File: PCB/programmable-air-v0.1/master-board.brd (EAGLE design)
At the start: 101.7 x 50.9 mm, 14 parts, among them J1 POWER_JACKTOE, Q1 600mA/40V, Q2 600mA/40V

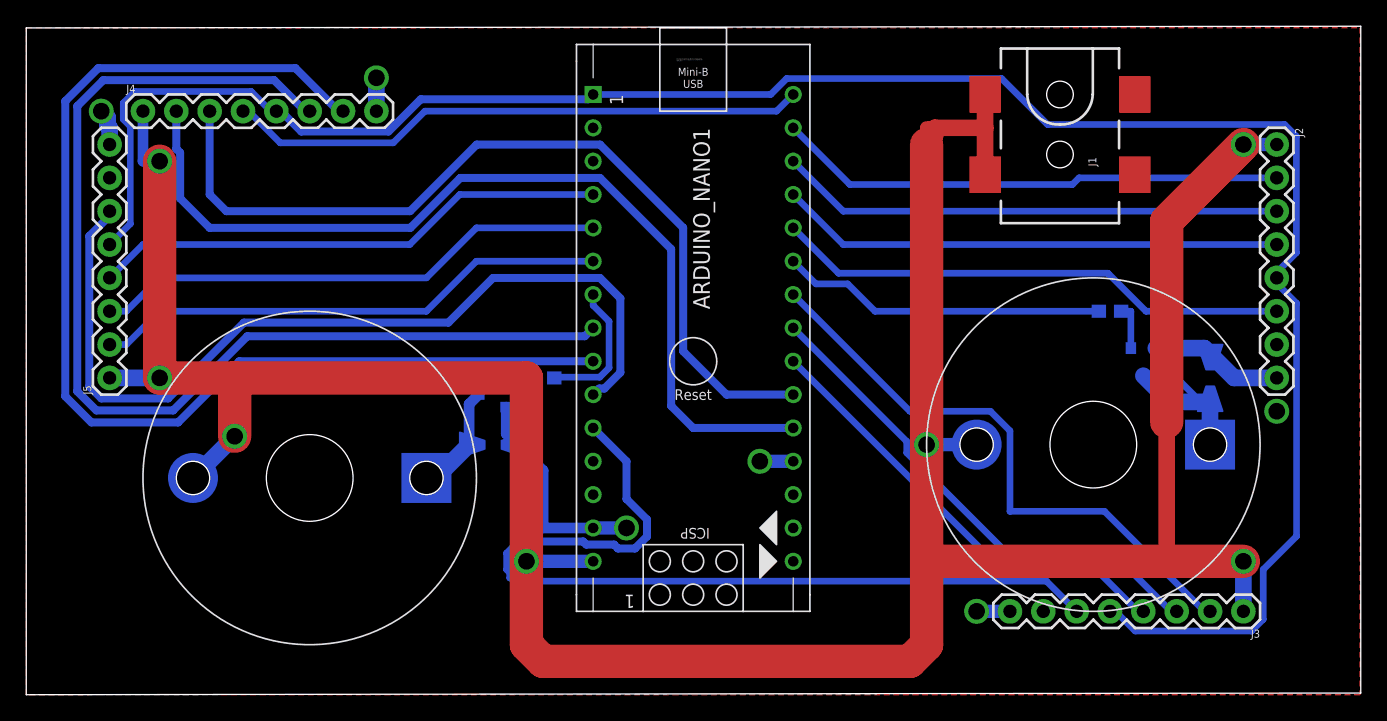
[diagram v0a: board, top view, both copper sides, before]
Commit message: Started work on slave PCB. Made changes to master pcb after testing
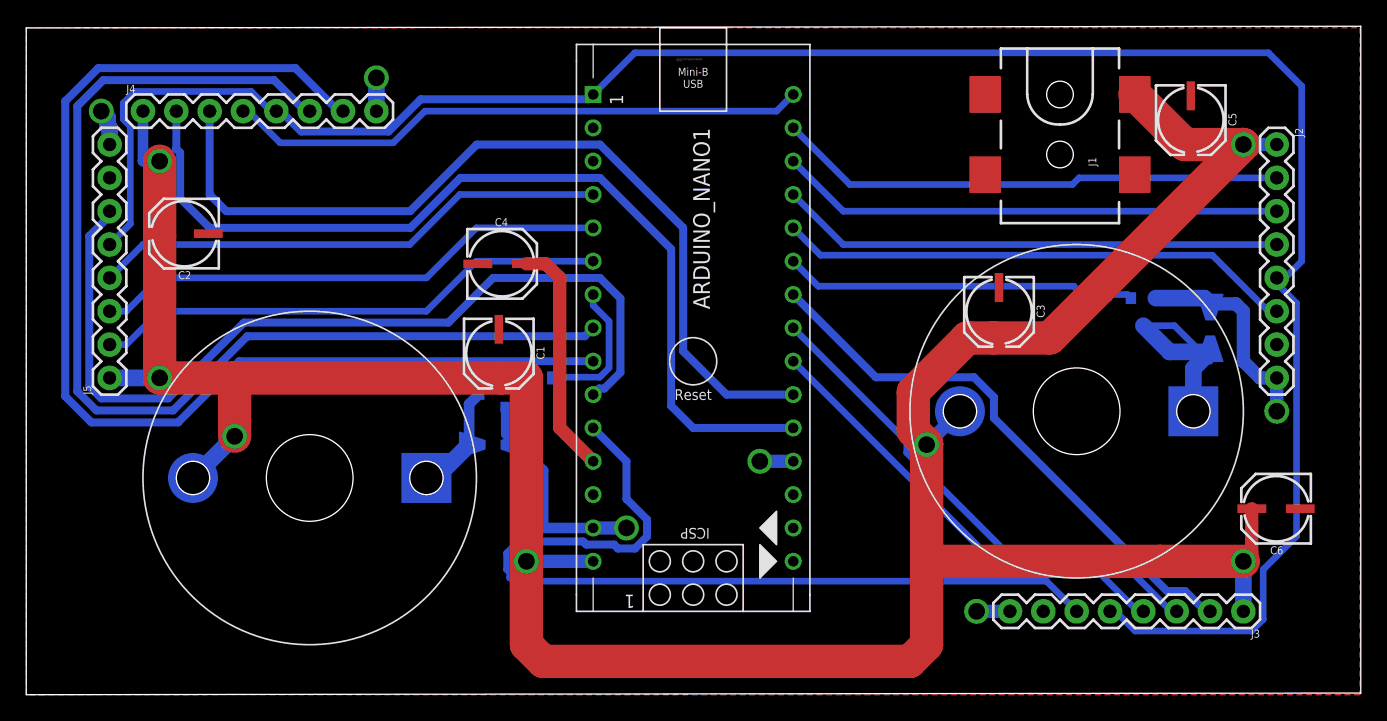
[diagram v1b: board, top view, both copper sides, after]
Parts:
- added C1, C2, C3, C4, C5, C6: 22uF, SparkFun-Capacitors:PANASONIC_C
- moved Q1 3.81 mm to (85.1, 29.2)
- moved U$4 3.81 mm to (90.2, 27.9)
- moved U$2 2.84 mm to (80.0, 21.6)
- moved R2 1.80 mm to (81.3, 30.5)
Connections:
- removed net 5V: ARDUINO_NANO1.12
- new net N$20: ARDUINO_NANO1.12, C4.+
- net GND: now also C1.-, C2.-, C3.-, C4.-, C5.-, C6.-, J1.GND, J1.P$4; no longer J1.VIN0
- net VIN: now also C1.+, C2.+, C3.+, C5.+, C6.+, J1.VIN0; no longer J1.GND, J1.P$4
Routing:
- net N$20: track 0.00 -> 18.0 mm
- net VIN: track 238.4 -> 221.9 mm
- net GND: track 37.3 -> 43.6 mm
- net N$13: track 157.9 -> 162.7 mm
- net N$9: track 45.3 -> 42.7 mm
- net N$1: track 24.9 -> 23.1 mm
- net N$6: track 15.4 -> 17.2 mm
- net N$7: track 3.55 -> 2.12 mm

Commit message: PCB v0.11 master ready for production
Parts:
- removed Q1, Q2: 600mA/40V, SparkFun-DiscreteSemi:SOT23-3
- added U$5, U$6: TIP120-TO220, programmable-air-components:TO220
- moved C3 23.0 mm to (63.5, 8.89)
- moved R2 19.1 mm to (62.2, 31.1)
- moved U$4 15.3 mm to (80.0, 16.5), turned to 0 degrees
- moved U$3 9.09 mm to (26.7, 21.0)
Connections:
- net GND: now also U$5.P$3, U$6.P$3; no longer Q1.2, Q2.2, U$3.P$2, U$4.P$2
- net N$2: now also U$6.P$1; no longer Q2.1
- net N$5: now also U$3.P$2, U$6.P$2; no longer Q2.3, U$3.P$1
- net N$6: now also U$4.P$2, U$5.P$2; no longer Q1.3, U$4.P$1
- net N$7: now also U$5.P$1; no longer Q1.1
- net VIN: now also U$3.P$1, U$4.P$1
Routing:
- net N$15: track 68.1 -> 42.6 mm
- net N$6: track 17.2 -> 39.5 mm
- net N$2: track 2.09 -> 22.0 mm
- net N$1: track 23.1 -> 3.75 mm
- net N$5: track 8.42 -> 21.2 mm
- net GND: track 43.6 -> 50.9 mm, vias 6 -> 7
- net VIN: track 221.9 -> 229.0 mm
- net N$9: track 42.7 -> 49.0 mm
- net N$4: track 38.7 -> 44.7 mm
- net N$3: track 34.6 -> 40.5 mm
- net N$22: track 39.5 -> 43.6 mm
- net N$23: track 38.4 -> 40.5 mm
- net N$24: track 38.4 -> 39.5 mm
- net N$7: track 2.12 -> 2.63 mm

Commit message: Forgot to add 5V input to slave boards
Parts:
- moved C6 0.90 mm to (95.9, 14.6), turned to 270 degrees
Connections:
- removed net N$12: ARDUINO_NANO1.9, J4.7
- net N$20: now also J2.7, J3.7, J4.7, J5.7
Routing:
- net N$20: track 18.0 -> 164.9 mm, vias 0 -> 2
- net N$12: track 89.0 -> 0.00 mm
- net GND: track 50.9 -> 23.8 mm, vias 7 -> 8
- net N$11: track 83.7 -> 85.0 mm
- net VIN: track 229.0 -> 228.7 mm, vias 7 -> 8
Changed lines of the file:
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@@
 <setting verticaltext="up"/>
 </settings>
-<grid distance="25" unitdist="mil" unit="mil" style="lines" multiple="1" display="yes" altdistance="5" altunitdist="mil" altunit="mil"/>
+<grid distance="50" unitdist="mil" unit="mil" style="lines" multiple="1" display="yes" altdistance="5" altunitdist="mil" altunit="mil"/>
 <layers>
 <layer number="1" name="Top" color="4" fill="1" visible="yes" active="yes"/>
@@
 <attribute name="PROD_ID" value="CAP-08618" x="88.9" y="43.815" size="1.778" layer="27" rot="R270" display="off"/>
 </element>
-<element name="C6" library="SparkFun-Capacitors" package="PANASONIC_C" value="22uF" x="95.25" y="13.97" rot="R180">
-<attribute name="PROD_ID" value="CAP-08618" x="95.25" y="13.97" size="1.778" layer="27" rot="R180" display="off"/>
+<element name="C6" library="SparkFun-Capacitors" package="PANASONIC_C" value="22uF" x="95.885" y="14.605" rot="R270">
+<attribute name="PROD_ID" value="CAP-08618" x="95.885" y="14.605" size="1.778" layer="27" rot="R270" display="off"/>
 </element>
 <element name="U$5" library="programmable-air-components" package="TO220" value="TIP120-TO220" x="65.405" y="33.655"/>
@@
 <contactref element="U$6" pad="P$3"/>
 <contactref element="U$5" pad="P$3"/>
-<wire x1="93.345" y1="24.13" x2="94.9325" y2="24.13" width="2.54" layer="16"/>
-<wire x1="83.82" y1="33.655" x2="93.345" y2="24.13" width="2.54" layer="16"/>
 <via x="27.94" y="3.175" extent="1-16" drill="1.27"/>
 <wire x1="32.385" y1="3.175" x2="27.94" y2="3.175" width="1.27" layer="16"/>
-<wire x1="67.945" y1="33.655" x2="83.82" y2="33.655" width="1.27" layer="16"/>
+<via x="71.755" y="33.655" extent="1-16" drill="1.27"/>
+<wire x1="67.945" y1="33.655" x2="71.755" y2="33.655" width="1.27" layer="16"/>
 </signal>
 <signal name="N$11">
@@
 <wire x1="18.8789875" y1="46.8122" x2="5.86805625" y2="46.8122" width="0.6096" layer="16"/>
 <wire x1="5.86805625" y1="46.8122" x2="3.8862" y2="44.83034375" width="0.6096" layer="16"/>
-<wire x1="3.8862" y1="44.83034375" x2="3.8862" y2="23.10945" width="0.6096" layer="16"/>
 <wire x1="42.545" y1="27.305" x2="43.18" y2="27.94" width="0.6096" layer="16"/>
 <wire x1="16.83730625" y1="27.305" x2="42.545" y2="27.305" width="0.6096" layer="16"/>
-</signal>
-<signal name="N$12">
-<contactref element="ARDUINO_NANO1" pad="9"/>
-<contactref element="J4" pad="7"/>
-<wire x1="5.48929375" y1="47.7266" x2="2.9718" y2="45.20910625" width="0.6096" layer="16"/>
-<wire x1="2.9718" y1="45.20910625" x2="2.9718" y2="22.7306875" width="0.6096" layer="16"/>
-<wire x1="2.9718" y1="22.7306875" x2="4.9633875" y2="20.7391" width="0.6096" layer="16"/>
-<wire x1="4.9633875" y1="20.7391" x2="11.56456875" y2="20.7391" width="0.6096" layer="16"/>
-<wire x1="24.13" y1="44.45" x2="23.7811875" y2="44.45" width="0.6096" layer="16"/>
-<wire x1="11.56456875" y1="20.7391" x2="16.22546875" y2="25.4" width="0.6096" layer="16"/>
-<wire x1="16.22546875" y1="25.4" x2="43.18" y2="25.4" width="0.6096" layer="16"/>
-<wire x1="23.7811875" y1="44.45" x2="20.5045875" y2="47.7266" width="0.6096" layer="16"/>
-<wire x1="20.5045875" y1="47.7266" x2="5.48929375" y2="47.7266" width="0.6096" layer="16"/>
+<wire x1="2.2987" y1="39.99600625" x2="2.2987" y2="38.74399375" width="0.508" layer="16"/>
+<wire x1="3.8862" y1="44.83034375" x2="3.8862" y2="41.58350625" width="0.508" layer="16"/>
+<wire x1="3.8862" y1="41.58350625" x2="2.2987" y2="39.99600625" width="0.508" layer="16"/>
+<wire x1="2.2987" y1="38.74399375" x2="3.81" y2="37.23269375" width="0.508" layer="16"/>
+<wire x1="3.81" y1="23.18565" x2="3.8862" y2="23.10945" width="0.508" layer="16"/>
+<wire x1="3.81" y1="37.23269375" x2="3.81" y2="23.18565" width="0.508" layer="16"/>
 </signal>
 <signal name="N$13">
@@
 <wire x1="40.64" y1="10.16" x2="43.18" y2="10.16" width="1.016" layer="16"/>
 <wire x1="10.16" y1="26.035" x2="10.16" y2="34.925" width="2.54" layer="1"/>
-<wire x1="10.16" y1="34.925" x2="10.16" y2="40.64" width="2.54" layer="1"/>
+<wire x1="10.16" y1="34.925" x2="10.16" y2="37.465" width="2.54" layer="1"/>
 <wire x1="86.868" y1="10.16" x2="86.36" y2="10.16" width="1.27" layer="1"/>
-<via x="10.16" y="40.64" extent="1-16" drill="1.27"/>
-<wire x1="10.16" y1="40.64" x2="8.89" y2="40.64" width="0.8128" layer="16"/>
+<via x="10.16" y="37.465" extent="1-16" drill="1.27"/>
+<wire x1="10.16" y1="37.465" x2="8.89" y2="40.64" width="0.8128" layer="16"/>
 <wire x1="8.89" y1="40.64" x2="8.89" y2="44.45" width="0.8128" layer="16"/>
 <via x="15.875" y="19.685" extent="1-16" drill="1.27"/>
@@
 <wire x1="88.25" y1="41.91" x2="92.71" y2="41.91" width="2.54" layer="1"/>
 <wire x1="92.71" y1="10.16" x2="86.36" y2="10.16" width="2.54" layer="1"/>
-<wire x1="68.58" y1="19.05" x2="68.58" y2="10.16" width="2.54" layer="1"/>
+<wire x1="68.58" y1="13.335" x2="68.58" y2="10.16" width="2.54" layer="1"/>
 <wire x1="67.564" y1="23.06294375" x2="67.564" y2="20.11705625" width="2.54" layer="1"/>
 <wire x1="67.564" y1="20.11705625" x2="68.58" y2="19.10105625" width="2.54" layer="1"/>
@@
 <contactref element="C5" pad="+"/>
 <contactref element="C6" pad="+"/>
-<wire x1="93.35" y1="14.17" x2="93.35" y2="10.8" width="1.016" layer="1"/>
 <wire x1="93.35" y1="10.8" x2="92.71" y2="10.16" width="1.016" layer="1"/>
 <wire x1="88.7" y1="41.915" x2="88.255" y2="41.915" width="0.6096" layer="1"/>
@@
 <wire x1="6.35" y1="24.13" x2="8.255" y2="24.13" width="2.54" layer="1"/>
 <wire x1="8.255" y1="24.13" x2="10.16" y2="26.035" width="2.54" layer="1"/>
+<via x="68.58" y="13.335" extent="1-16" drill="1.27"/>
+<wire x1="68.58" y1="13.335" x2="68.58" y2="19.05" width="2.54" layer="16"/>
+<wire x1="95.685" y1="12.705" x2="93.14" y2="10.16" width="1.27" layer="1"/>
+<wire x1="93.14" y1="10.16" x2="92.71" y2="10.16" width="1.27" layer="1"/>
 </signal>
 <signal name="N$8">
@@
 <contactref element="ARDUINO_NANO1" pad="12"/>
 <contactref element="C4" pad="+"/>
-<wire x1="38.095" y1="32.82" x2="39.57" y2="32.82" width="1.016" layer="1"/>
-<wire x1="39.57" y1="32.82" x2="40.64" y2="31.75" width="1.016" layer="1"/>
-<wire x1="40.64" y1="20.32" x2="43.18" y2="17.78" width="1.016" layer="1"/>
-<wire x1="40.64" y1="31.75" x2="40.64" y2="20.32" width="1.016" layer="1"/>
+<wire x1="38.095" y1="32.82" x2="38.735" y2="32.82" width="1.016" layer="1"/>
+<wire x1="38.735" y1="32.82" x2="39.57" y2="32.82" width="1.016" layer="1"/>
+<contactref element="J5" pad="7"/>
+<contactref element="J4" pad="7"/>
+<contactref element="J3" pad="7"/>
+<contactref element="J2" pad="7"/>
+<wire x1="24.13" y1="44.45" x2="24.13" y2="46.99" width="1.27" layer="1"/>
+<wire x1="6.35" y1="39.37" x2="8.93986875" y2="39.37" width="1.27" layer="1"/>
+<wire x1="8.93986875" y1="39.37" x2="9.24466875" y2="39.6748" width="1.27" layer="1"/>
+<wire x1="24.13" y1="40.64" x2="23.1648" y2="39.6748" width="1.27" layer="1"/>
+<wire x1="23.1648" y1="39.6748" x2="9.24466875" y2="39.6748" width="1.27" layer="1"/>
+<wire x1="6.35" y1="39.37" x2="3.81" y2="39.37" width="1.27" layer="1"/>
+<wire x1="43.18" y1="17.78" x2="46.3677" y2="14.5923" width="1.27" layer="16"/>
+<wire x1="46.3677" y1="14.5923" x2="46.50381875" y2="14.5923" width="1.27" layer="16"/>
+<wire x1="57.28611875" y1="3.81" x2="76.835" y2="3.81" width="1.27" layer="16"/>
+<wire x1="46.50381875" y1="14.5923" x2="57.28611875" y2="3.81" width="1.27" layer="16"/>
+<wire x1="76.835" y1="3.81" x2="76.835" y2="5.715" width="1.27" layer="16"/>
+<wire x1="76.835" y1="5.715" x2="77.47" y2="6.35" width="1.27" layer="16"/>
+<wire x1="24.13" y1="44.45" x2="24.13" y2="40.64" width="1.27" layer="1"/>
+<wire x1="24.13" y1="40.64" x2="24.765" y2="40.005" width="1.27" layer="1"/>
+<wire x1="24.765" y1="40.005" x2="36.83" y2="40.005" width="1.27" layer="1"/>
+<wire x1="36.83" y1="40.005" x2="38.735" y2="38.1" width="1.27" layer="1"/>
+<wire x1="38.735" y1="38.1" x2="38.735" y2="32.82" width="1.27" layer="1"/>
+<wire x1="41.91" y1="31.75" x2="45.085" y2="31.75" width="0.508" layer="1"/>
+<wire x1="45.085" y1="17.78" x2="45.085" y2="31.75" width="1.016" layer="1"/>
+<wire x1="43.18" y1="17.78" x2="45.085" y2="17.78" width="1.016" layer="1"/>
+<wire x1="38.095" y1="32.82" x2="39.165" y2="31.75" width="1.016" layer="1"/>
+<wire x1="39.165" y1="31.75" x2="41.91" y2="31.75" width="1.016" layer="1"/>
+<via x="3.81" y="39.37" extent="1-16" drill="1.27"/>
+<via x="24.13" y="46.99" extent="1-16" drill="1.27"/>
+<wire x1="77.47" y1="6.35" x2="77.47" y2="3.81" width="1.27" layer="1"/>
+<wire x1="77.47" y1="3.81" x2="96.52" y2="3.81" width="1.27" layer="1"/>
+<wire x1="96.52" y1="3.81" x2="100" y2="7.29" width="1.27" layer="1"/>
+<wire x1="100" y1="25.095" x2="98.425" y2="26.67" width="1.27" layer="1"/>
+<wire x1="98.425" y1="26.67" x2="95.25" y2="26.67" width="1.27" layer="1"/>
+<wire x1="100" y1="7.29" x2="100" y2="25.095" width="1.27" layer="1"/>
 </signal>
 </signals>
